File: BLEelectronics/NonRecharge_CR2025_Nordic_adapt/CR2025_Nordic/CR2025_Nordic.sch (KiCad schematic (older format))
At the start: 24 parts, among them J1 USB_A_PLUG, J2 AU-Y1006-R, Q1 Si2307CDS, U1 TPD2E2U06, U2 BAT-HLD-001, U3 LTC4412xS6, U4 LTC4054LES5-4.2#TRPBF, U5 MX25R6435FM2IL0

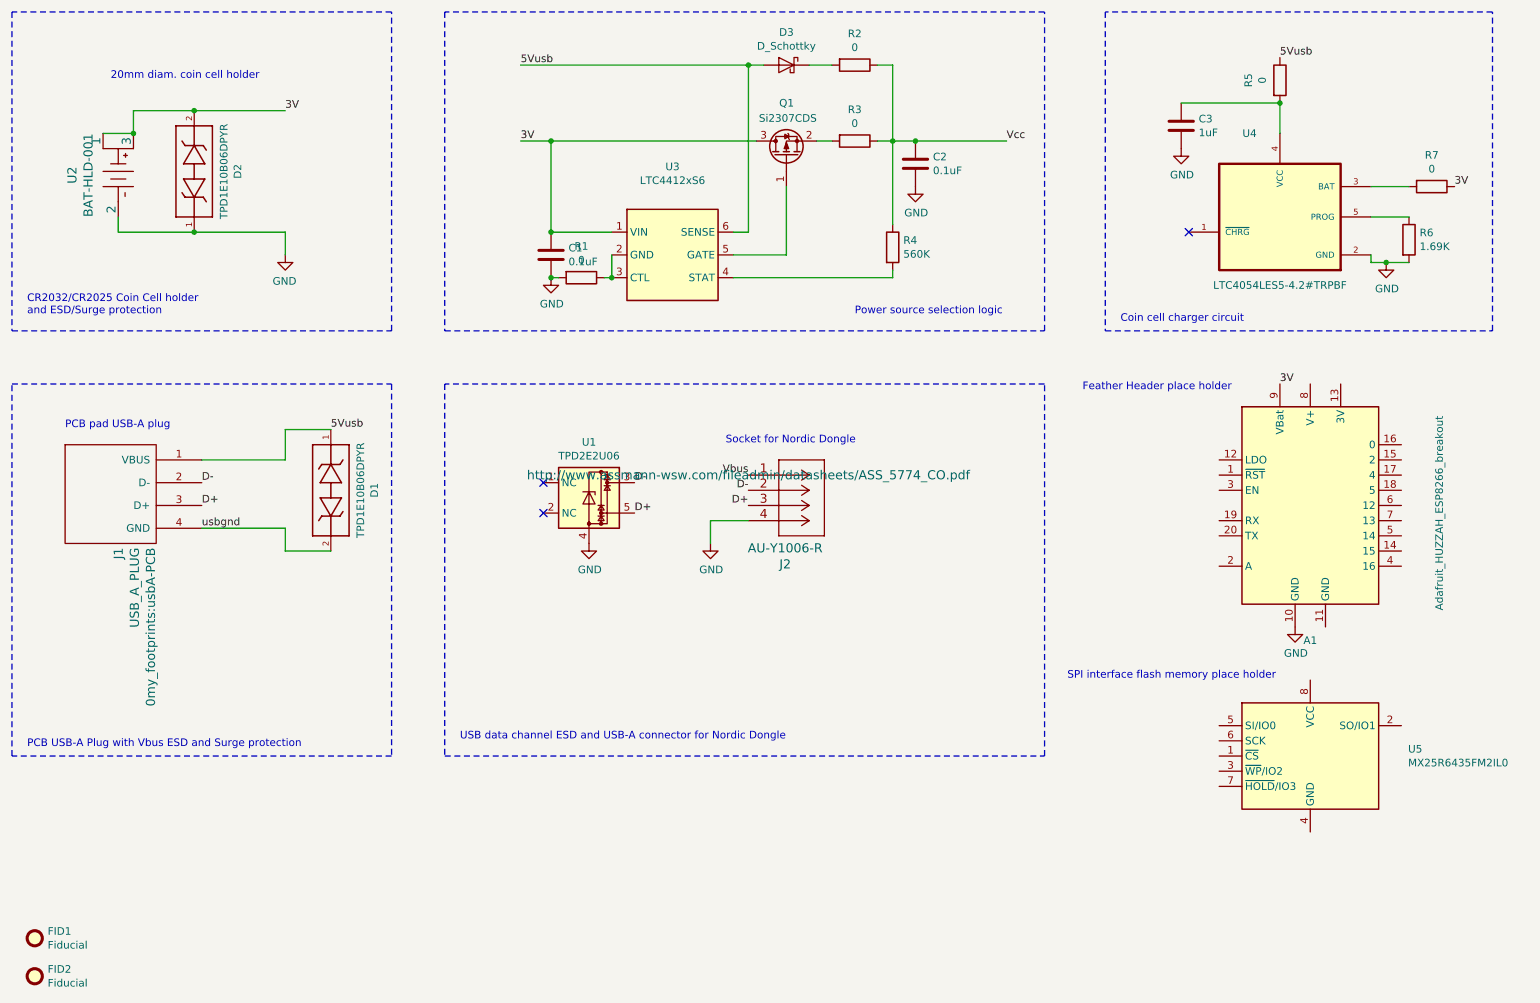
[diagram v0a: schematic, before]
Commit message: added LP5970 .3V regulator to 5USB input. Created custom Nordic nRF52840 header. Todo: layout and pack libraries.
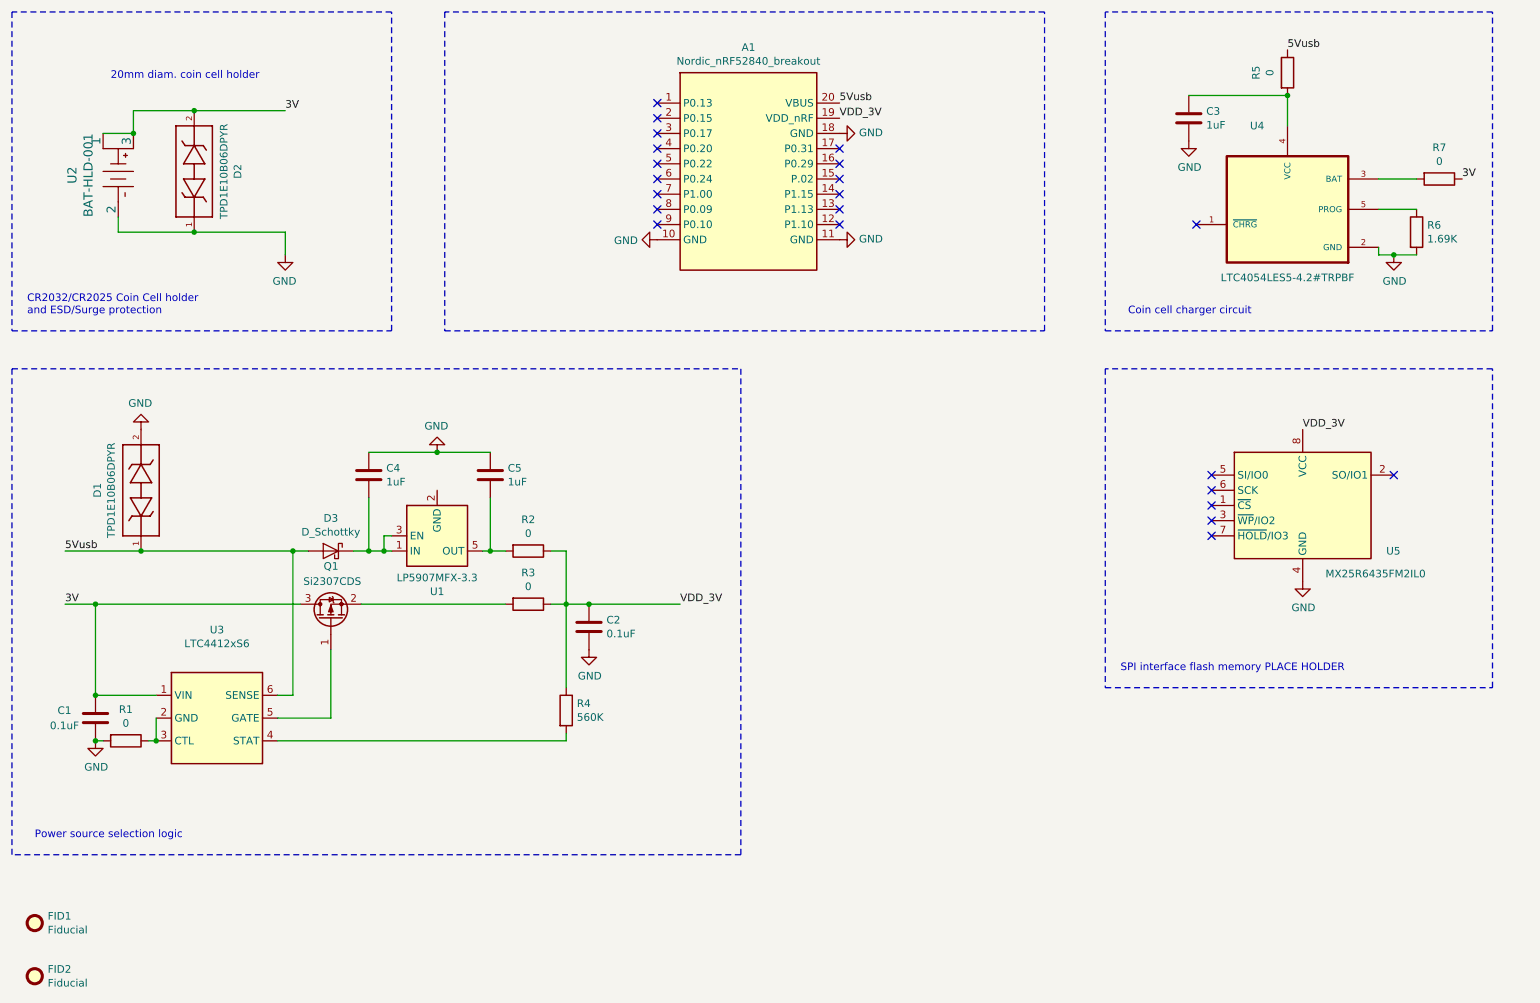
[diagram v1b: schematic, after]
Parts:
- removed A1: Adafruit_HUZZAH_ESP8266_breakout, Module:Adafruit_HUZZAH_ESP8266_breakout, symbol MCU_Module:Adafruit_HUZZAH_ESP8266_breakout
- removed J1: USB_A_PLUG, 0my_footprints:usbA-PCB, symbol usb_a_plug:USB_A_PLUG
- removed J2: AU-Y1006-R, 0my_footprints:AU-Y1006-R, symbol AU-Y1006-R:AU-Y1006-R
- removed U1: TPD2E2U06, Package_TO_SOT_SMD:SOT-543, symbol Power_Protection:TPD2E2U06
- added A1: Nordic_nRF52840_breakout, Module:Adafruit_HUZZAH_ESP8266_breakout, symbol MCU_Module:Nordic_nRF52840_breakout
- added C4, C5: 1uF, Capacitor_SMD:C_0603_1608Metric_Pad1.05x0.95mm_HandSolder, symbol Device:C
- added U1: LP5907MFX-3.3, Package_TO_SOT_SMD:SOT-23-5, symbol Regulator_Linear:LP5907MFX-3.3
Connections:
- net Vcc is gone; now on net VDD_3V: C2.1, R2.1, R3.1, R4.1
- net usbgnd is gone; now on net GND: D1.2
- net 5Vusb: now also A1.20 (VBUS)
- net GND: now also U5.4 (GND), A1.10 (GND), A1.11 (GND), A1.18 (GND), C4.1, C5.1
- net at D3.1 (K): now also C4.2, U1.1 (IN), U1.3 (EN); no longer R2.2
- net VDD_3V: now reaches U5.8 (VCC)
- net VDD_3V: now also A1.19 (VDD_nRF)
- new net: C5.2, R2.2, U1.5 (OUT)
- no-connect marks 3 -> 22
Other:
- note added: "SPI interface flash memory PLACE HOLDER"
- note removed: "Feather Header place holder\n"
- note removed: "PCB USB-A Plug with Vbus ESD and Surge protection"
- note removed: "PCB pad USB-A plug"
- note removed: "SPI interface flash memory place holder"
- note removed: "Socket for Nordic Dongle"
- note removed: "USB data channel ESD and USB-A connector for Nordic Dongle\n"
- moved on the sheet: C1, C2, C3, D1, D3, FID1, Q1, R1, R2, R3, R4, R5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
